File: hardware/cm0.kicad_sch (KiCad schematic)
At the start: 0 parts

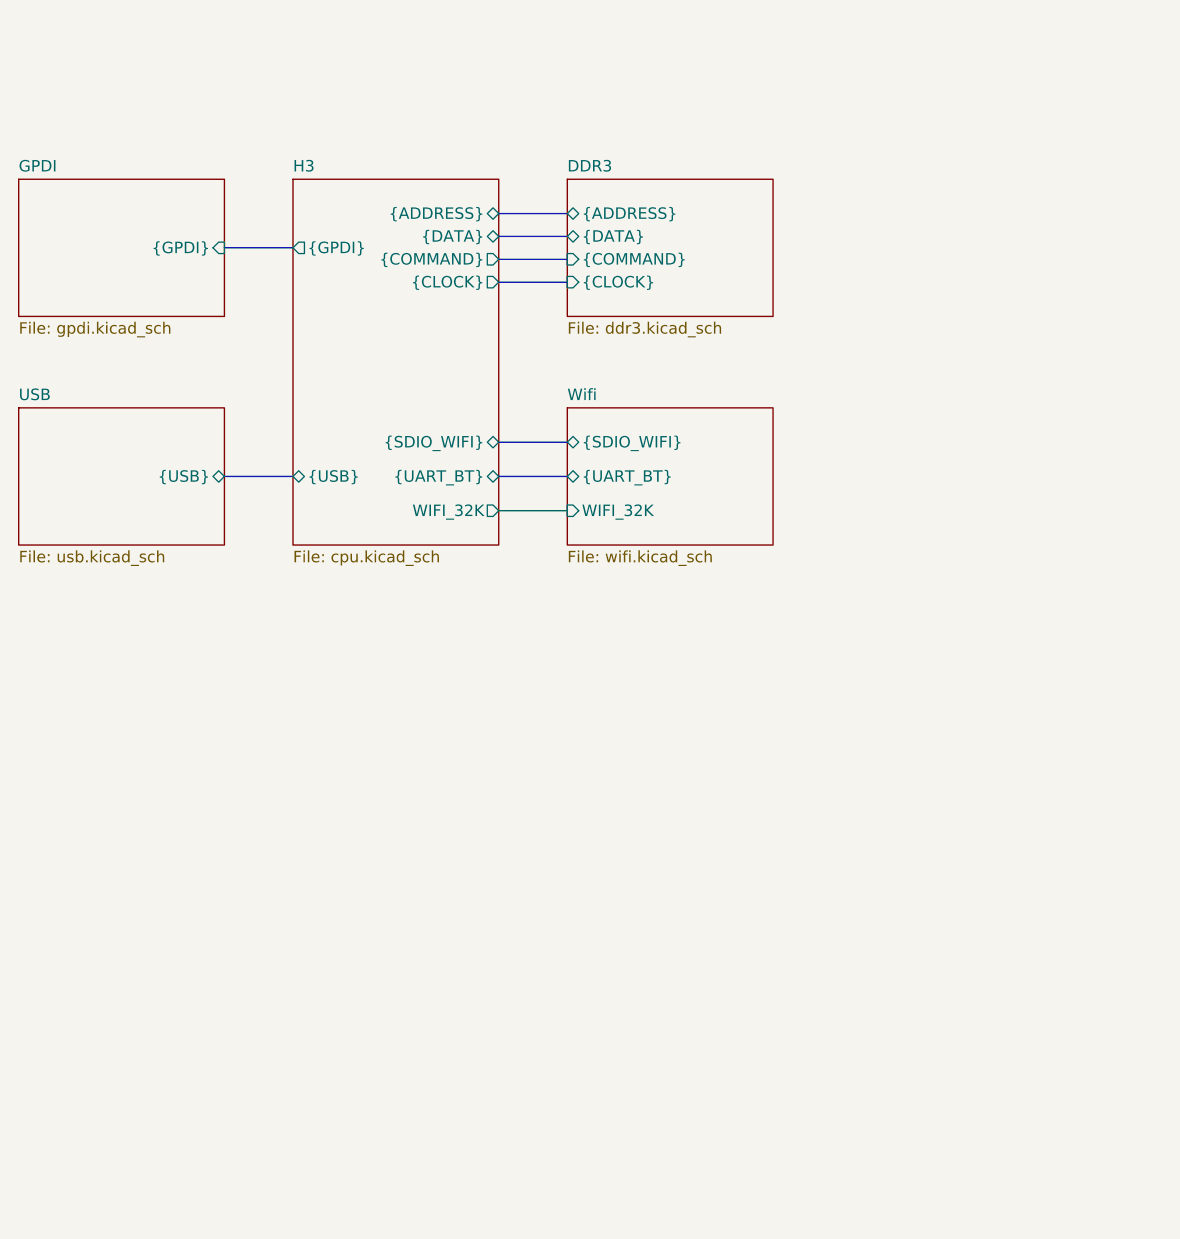
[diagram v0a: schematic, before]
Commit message: Added TVS diodes, RF switch and changed RJ45 conn
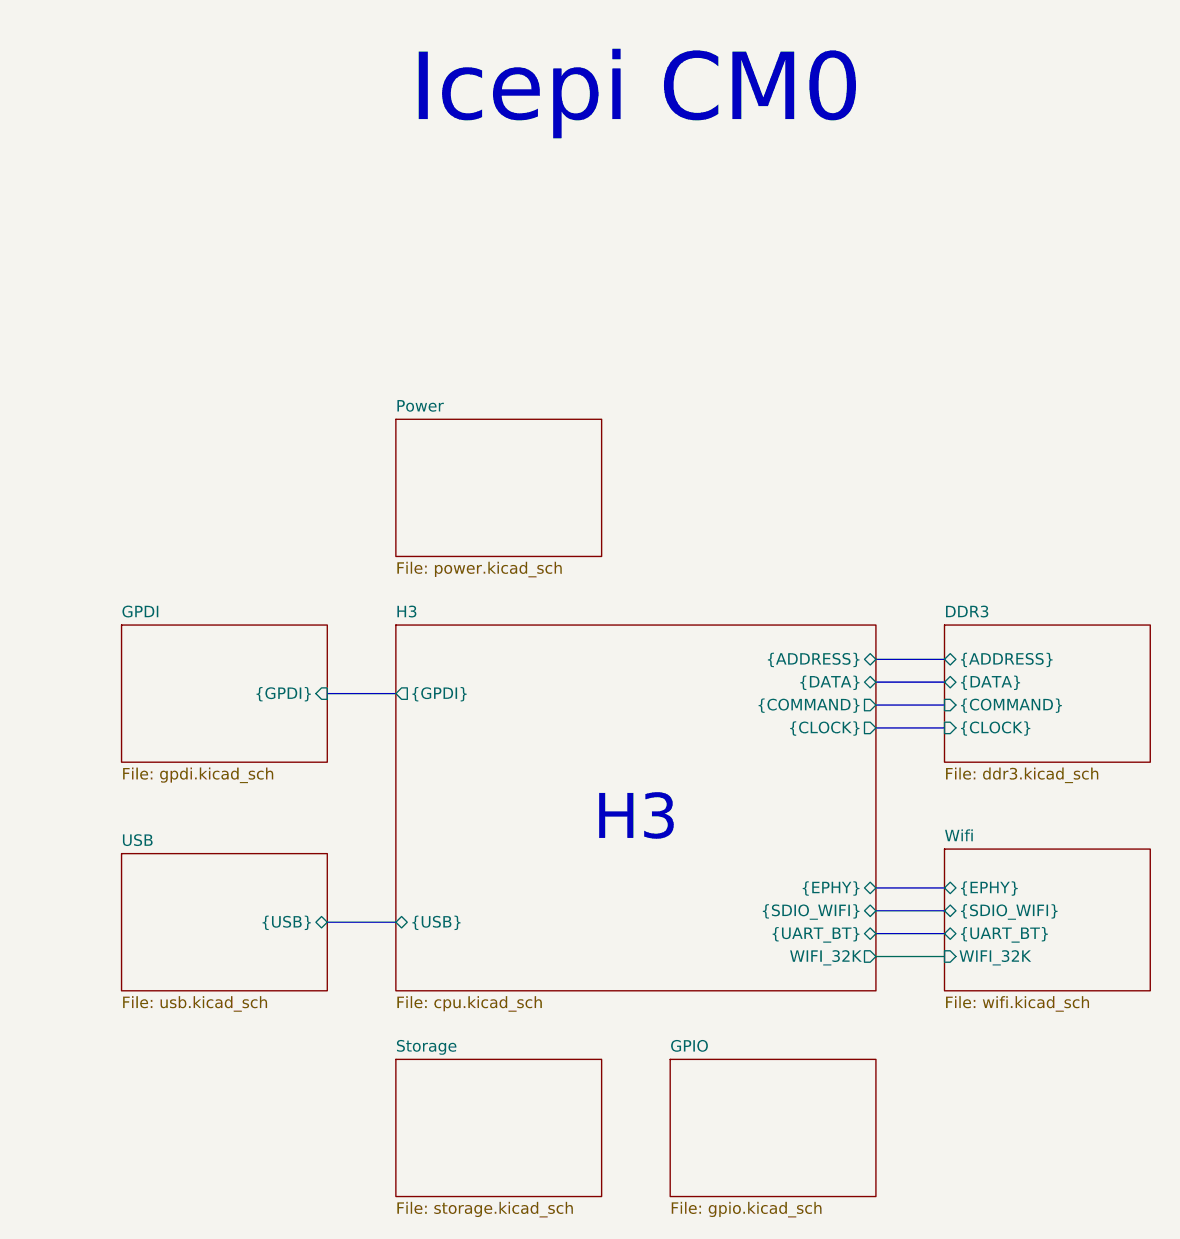
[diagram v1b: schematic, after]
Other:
- added sheet GPIO (gpio.kicad_sch)
- added sheet Power (power.kicad_sch)
- added sheet Storage (storage.kicad_sch)
- sheet H3 ports: added {EPHY}; removed none
- sheet Wifi ports: added {EPHY}; removed none
- note added: "H3"
- note added: "Icepi CM0"
